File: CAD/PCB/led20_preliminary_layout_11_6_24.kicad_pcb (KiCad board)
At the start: 2 copper layers, 55 x 55 mm, 33 parts, among them U3 Battery, U6 JST

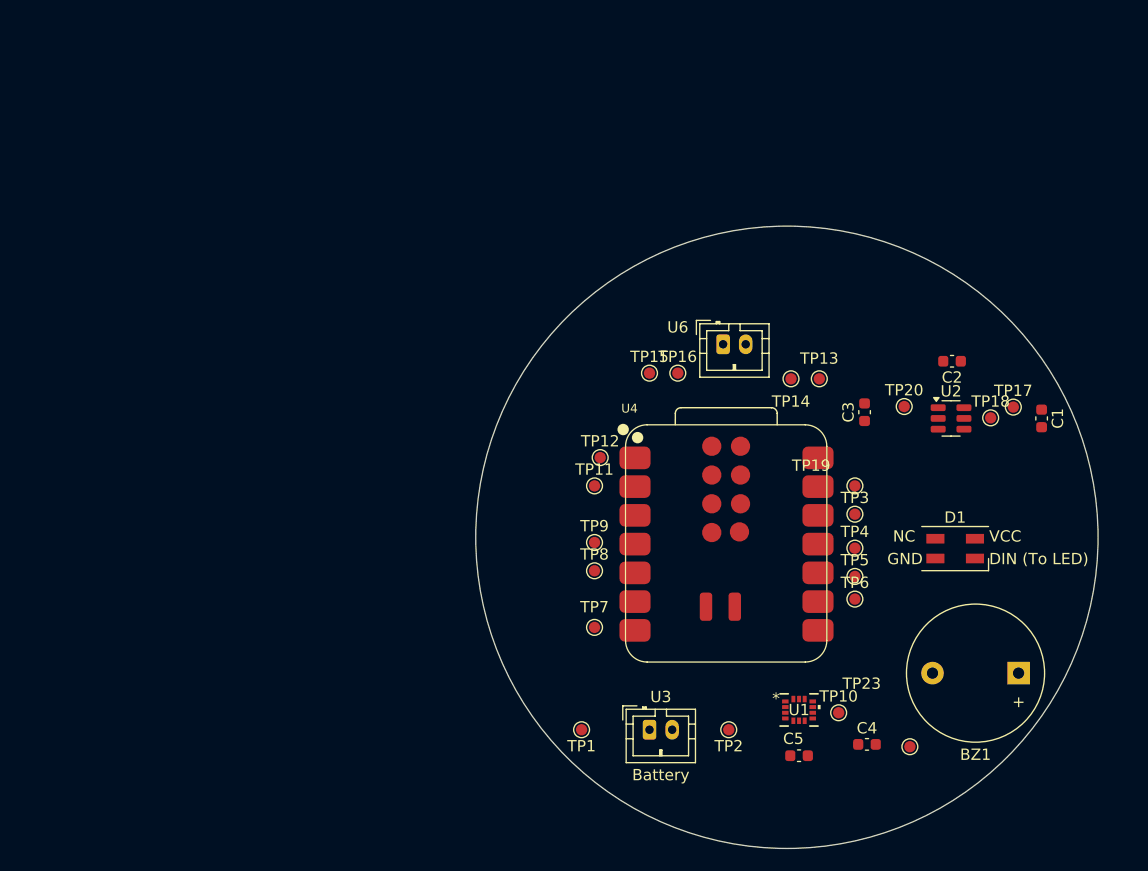
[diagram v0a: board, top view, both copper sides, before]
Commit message: Added Functional Decomposition
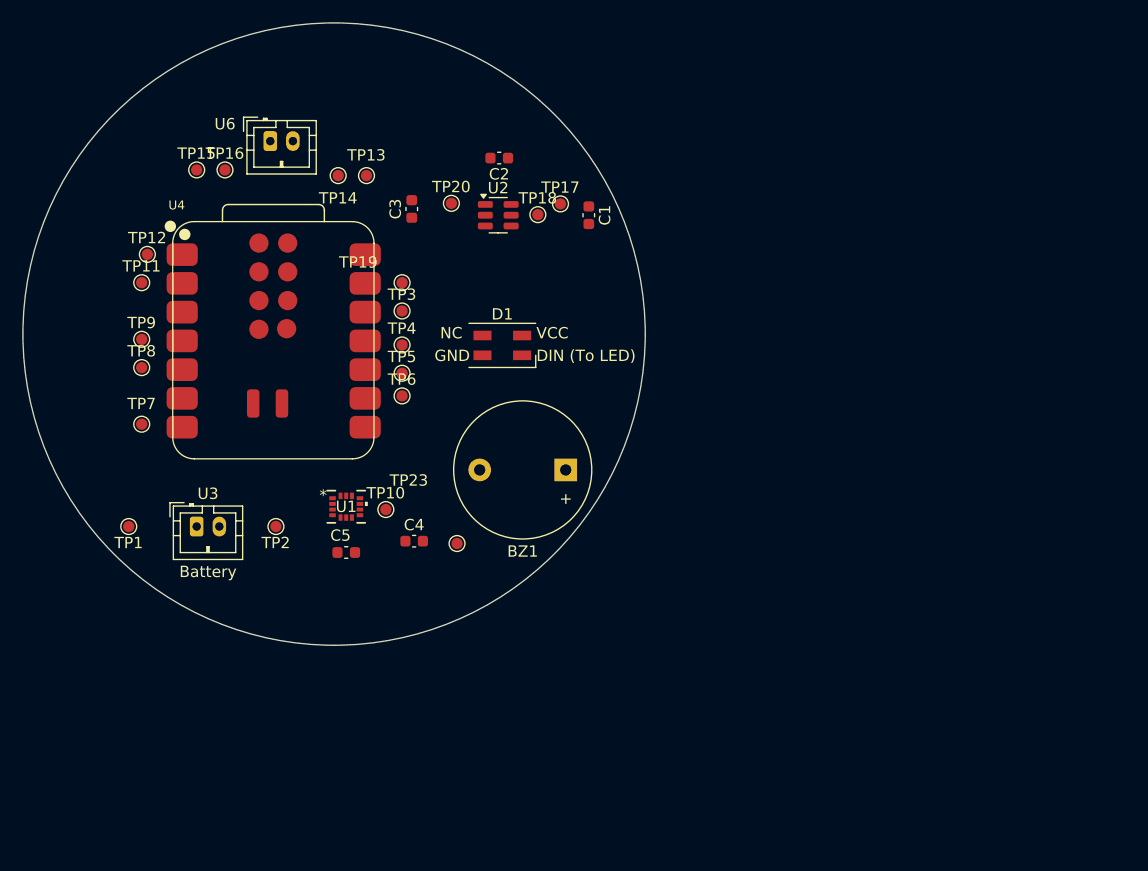
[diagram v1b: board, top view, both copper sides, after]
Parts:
- moved BZ1 43.8 mm to (123.6, 72.0)
- moved C2 43.8 mm to (117.7, 44.5)
- moved C3 43.8 mm to (110.0, 49.0)
- moved D1 43.8 mm to (118.0, 61.0)
- moved TP1 43.8 mm to (85.0, 77.0)
- moved TP11 43.8 mm to (86.1, 55.5)
- moved TP12 43.8 mm to (86.6, 53.0)
- moved TP13 43.8 mm to (106.0, 46.0)
- moved TP14 43.8 mm to (103.5, 46.0)
- moved TP15 43.8 mm to (91.0, 45.5)
- moved TP16 43.8 mm to (93.5, 45.5)
- moved TP2 43.8 mm to (98.0, 77.0)
- moved TP20 43.8 mm to (113.5, 48.5)
- moved TP23 43.8 mm to (114.0, 78.5)
- moved TP7 43.8 mm to (86.1, 68.0)
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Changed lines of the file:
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@@
 		(legacy_teardrops no)
 	)
-	(paper "A4")
+	(paper "A5")
 	(title_block
 		(title "LED20 Preliminary PCB Layout")
@@
 		(allow_soldermask_bridges_in_footprints no)
 		(pcbplotparams
-			(layerselection 0x0040000_7ffffffe)
+			(layerselection 0x0001000_7ffffffe)
 			(plot_on_all_layers_selection 0x7ffffff_80000001)
 			(disableapertmacros no)
@@
 			(drillshape 0)
 			(scaleselection 1)
-			(outputdirectory "")
+			(outputdirectory "./")
 		)
 	)
@@
 	(footprint "Connector_JST:JST_PH_B2B-PH-K_1x02_P2.00mm_Vertical"
 		(layer "F.Cu")
-		(at 137.5 60.95)
+		(at 97.5 43)
 		(descr "JST PH series connector, B2B-PH-K (http://www.jst-mfg.com/product/pdf/eng/ePH.pdf), generated with kicad-footprint-generator")
 		(tags "connector JST PH side entry")
@@
 	(footprint "TestPoint:TestPoint_Pad_D1.0mm"
 		(layer "F.Cu")
-		(at 138 95 180)
+		(at 98 77.05 180)
 		(descr "SMD pad as test Point, diameter 1.0mm")
 		(tags "test point SMD pad")
@@
 	(footprint "Led20:ChargePump"
 		(layer "F.Cu")
-		(at 157.6375 67.5)
+		(at 117.6375 49.55)
 		(descr "SOT, 6 Pin (~), generated with kicad-footprint-generator ipc_gullwing_generator.py")
 		(tags "SOT TO_SOT_SMD")
@@
 	(footprint "TestPoint:TestPoint_Pad_D1.0mm"
 		(layer "F.Cu")
-		(at 147.7103 93.499999)
+		(at 107.7103 75.549999)
 		(descr "SMD pad as test Point, diameter 1.0mm")
 		(tags "test point SMD pad")
@@
 	(footprint "TestPoint:TestPoint_Pad_D1.0mm"
 		(layer "F.Cu")
-		(at 154 96.5)
+		(at 114 78.55)
 		(descr "SMD pad as test Point, diameter 1.0mm")
 		(tags "test point SMD pad")
@@
 	(footprint "LED_SMD:LED_SK6812MINI_PLCC4_3.5x3.5mm_P1.75mm"
 		(layer "F.Cu")
-		(at 158 79)
+		(at 118 61.05)
 		(descr "3.5mm x 3.5mm PLCC4 Addressable RGB LED NeoPixel, https://cdn-shop.adafruit.com/product-files/2686/SK6812MINI_REV.01-1-2.pdf")
 		(tags "LED RGB NeoPixel Mini PLCC-4 3535")
@@
 	(footprint "Capacitor_SMD:C_0603_1608Metric"
 		(layer "F.Cu")
-		(at 150 66.95 90)
+		(at 110 49 90)
 		(descr "Capacitor SMD 0603 (1608 Metric), square (rectangular) end terminal, IPC_7351 nominal, (Body size source: IPC-SM-782 page 76, https://www.pcb-3d.com/wordpress/wp-content/uploads/ipc-sm-782a_amendment_1_and_2.pdf), generated with kicad-footprint-generator")
 		(tags "capacitor")
@@
 	(footprint "TestPoint:TestPoint_Pad_D1.0mm"
 		(layer "F.Cu")
-		(at 126.1444 80.96)
+		(at 86.1444 63.01)
 		(descr "SMD pad as test Point, diameter 1.0mm")
 		(tags "test point SMD pad")
@@
 	(footprint "TestPoint:TestPoint_Pad_D1.0mm"
 		(layer "F.Cu")
-		(at 131 63.5)
+		(at 91 45.55)
 		(descr "SMD pad as test Point, diameter 1.0mm")
 		(tags "test point SMD pad")
@@
 	(footprint "Connector_JST:JST_PH_B2B-PH-K_1x02_P2.00mm_Vertical"
 		(layer "F.Cu")
-		(at 131 95)
+		(at 91 77.05)
 		(descr "JST PH series connector, B2B-PH-K (http://www.jst-mfg.com/product/pdf/eng/ePH.pdf), generated with kicad-footprint-generator")
 		(tags "connector JST PH side entry")
@@
 	(footprint "TestPoint:TestPoint_Pad_D1.0mm"
 		(layer "F.Cu")
-		(at 133.5 63.5)
+		(at 93.5 45.55)
 		(descr "SMD pad as test Point, diameter 1.0mm")
 		(tags "test point SMD pad")
@@
 	(footprint "Capacitor_SMD:C_0603_1608Metric"
 		(layer "F.Cu")
-		(at 144.2103 97.293699)
+		(at 104.2103 79.343699)
 		(descr "Capacitor SMD 0603 (1608 Metric), square (rectangular) end terminal, IPC_7351 nominal, (Body size source: IPC-SM-782 page 76, https://www.pcb-3d.com/wordpress/wp-content/uploads/ipc-sm-782a_amendment_1_and_2.pdf), generated with kicad-footprint-generator")
 		(tags "capacitor")
@@
 	(footprint "Led20:LGA-14L_2P5X3X0P83_STM-L"
 		(layer "F.Cu")
-		(at 144.2103 93.249999)
+		(at 104.2103 75.299999)
 		(tags "LSM6DSO32TR ")
 		(property "Reference" "U1"
@@
 	(footprint "TestPoint:TestPoint_Pad_D1.0mm"
 		(layer "F.Cu")
-		(at 126.1444 85.96)
+		(at 86.1444 68.01)
 		(descr "SMD pad as test Point, diameter 1.0mm")
 		(tags "test point SMD pad")
@@
 	(footprint "Led20:XIAO-ESP32-C6-SMD"
 		(layer "F.Cu")
-		(at 138 78.58)
+		(at 98 60.63)
 		(property "Reference" "U4"
 			(at -9.5 -11.5 0)
@@
 	(footprint "TestPoint:TestPoint_Pad_D1.0mm"
 		(layer "F.Cu")
-		(at 146 64)
+		(at 106 46.05)
 		(descr "SMD pad as test Point, diameter 1.0mm")
 		(tags "test point SMD pad")
@@
 	(footprint "TestPoint:TestPoint_Pad_D1.0mm"
 		(layer "F.Cu")
-		(at 161.1375 67.45)
+		(at 121.1375 49.5)
 		(descr "SMD pad as test Point, diameter 1.0mm")
 		(tags "test point SMD pad")
@@
 	(footprint "Capacitor_SMD:C_0603_1608Metric"
 		(layer "F.Cu")
-		(at 165.6375 67.5 -90)
+		(at 125.6375 49.55 -90)
 		(descr "Capacitor SMD 0603 (1608 Metric), square (rectangular) end terminal, IPC_7351 nominal, (Body size source: IPC-SM-782 page 76, https://www.pcb-3d.com/wordpress/wp-content/uploads/ipc-sm-782a_amendment_1_and_2.pdf), generated with kicad-footprint-generator")
 		(tags "capacitor")
@@
 	(footprint "Buzzer_Beeper:Buzzer_12x9.5RM7.6"
 		(layer "F.Cu")
-		(at 163.6 90 180)
+		(at 123.6 72.05 180)
 		(descr "Generic Buzzer, D12mm height 9.5mm with RM7.6mm")
 		(tags "buzzer")
@@
 	(footprint "TestPoint:TestPoint_Pad_D1.0mm"
 		(layer "F.Cu")
-		(at 143.5 64)
+		(at 103.5 46.05)
 		(descr "SMD pad as test Point, diameter 1.0mm")
 		(tags "test point SMD pad")
@@
 	(footprint "TestPoint:TestPoint_Pad_D1.0mm"
 		(layer "F.Cu")
-		(at 125 95 180)
+		(at 85 77.05 180)
 		(descr "SMD pad as test Point, diameter 1.0mm")
 		(tags "test point SMD pad")
@@
 	(footprint "Capacitor_SMD:C_0603_1608Metric"
 		(layer "F.Cu")
-		(at 157.725 62.45 180)
+		(at 117.725 44.5 180)
 		(descr "Capacitor SMD 0603 (1608 Metric), square (rectangular) end terminal, IPC_7351 nominal, (Body size source: IPC-SM-782 page 76, https://www.pcb-3d.com/wordpress/wp-content/uploads/ipc-sm-782a_amendment_1_and_2.pdf), generated with kicad-footprint-generator")
 		(tags "capacitor")
@@
 	(footprint "TestPoint:TestPoint_Pad_D1.0mm"
 		(layer "F.Cu")
-		(at 163.1375 66.5)
+		(at 123.1375 48.55)
 		(descr "SMD pad as test Point, diameter 1.0mm")
 		(tags "test point SMD pad")
@@
 	(footprint "TestPoint:TestPoint_Pad_D1.0mm"
 		(layer "F.Cu")
-		(at 149.1444 78.96)
+		(at 109.1444 61.01)
 		(descr "SMD pad as test Point, diameter 1.0mm")
 		(tags "test point SMD pad")
@@
 	(footprint "TestPoint:TestPoint_Pad_D1.0mm"
 		(layer "F.Cu")
-		(at 153.5 66.45)
+		(at 113.5 48.5)
 		(descr "SMD pad as test Point, diameter 1.0mm")
 		(tags "test point SMD pad")
@@
 	(footprint "TestPoint:TestPoint_Pad_D1.0mm"
 		(layer "F.Cu")
-		(at 149.1444 75.96)
+		(at 109.1444 58.01)
 		(descr "SMD pad as test Point, diameter 1.0mm")
 		(tags "test point SMD pad")
@@
 	(footprint "TestPoint:TestPoint_Pad_D1.0mm"
 		(layer "F.Cu")
-		(at 149.1444 73.46)
+		(at 109.1444 55.51)
 		(descr "SMD pad as test Point, diameter 1.0mm")
 		(tags "test point SMD pad")
@@
 	(footprint "TestPoint:TestPoint_Pad_D1.0mm"
 		(layer "F.Cu")
-		(at 149.1444 83.46)
+		(at 109.1444 65.51)
 		(descr "SMD pad as test Point, diameter 1.0mm")
 		(tags "test point SMD pad")
@@
 	(footprint "TestPoint:TestPoint_Pad_D1.0mm"
 		(layer "F.Cu")
-		(at 126.6444 70.96)
+		(at 86.6444 53.01)
 		(descr "SMD pad as test Point, diameter 1.0mm")
 		(tags "test point SMD pad")
@@
 	(footprint "TestPoint:TestPoint_Pad_D1.0mm"
 		(layer "F.Cu")
-		(at 126.1444 73.46)
+		(at 86.1444 55.51)
 		(descr "SMD pad as test Point, diameter 1.0mm")
 		(tags "test point SMD pad")
@@
 	(footprint "TestPoint:TestPoint_Pad_D1.0mm"
 		(layer "F.Cu")
-		(at 149.1444 81.46)
+		(at 109.1444 63.51)
 		(descr "SMD pad as test Point, diameter 1.0mm")
 		(tags "test point SMD pad")
@@
 	(footprint "TestPoint:TestPoint_Pad_D1.0mm"
 		(layer "F.Cu")
-		(at 126.1444 78.46)
+		(at 86.1444 60.51)
 		(descr "SMD pad as test Point, diameter 1.0mm")
 		(tags "test point SMD pad")
@@
 	(footprint "Capacitor_SMD:C_0603_1608Metric"
 		(layer "F.Cu")
-		(at 150.2103 96.293699)
+		(at 110.2103 78.343699)
 		(descr "Capacitor SMD 0603 (1608 Metric), square (rectangular) end terminal, IPC_7351 nominal, (Body size source: IPC-SM-782 page 76, https://www.pcb-3d.com/wordpress/wp-content/uploads/ipc-sm-782a_amendment_1_and_2.pdf), generated with kicad-footprint-generator")
 		(tags "capacitor")
@@
 	)
 	(gr_circle
-		(center 143.1375 78)
-		(end 163 59)
+		(center 103.1375 60.05)
+		(end 123 41.05)
 		(stroke
 			(width 0.05)
@@
 	)
 	(gr_text "NC"
-		(at 152.5 78.5 0)
+		(at 112.5 60.55 0)
 		(layer "F.SilkS")
 		(effects
@@
 	)
 	(gr_text "DIN (To LED)\n"
-		(at 161 80.5 0)
+		(at 121 62.55 0)
 		(layer "F.SilkS")
 		(effects
@@
 	)
 	(gr_text "GND\n"
-		(at 152 80.5 0)
+		(at 112 62.55 0)
 		(layer "F.SilkS")
 		(effects
@@
 	)
 	(gr_text "VCC"
-		(at 161 78.5 0)
+		(at 121 60.55 0)
 		(layer "F.SilkS")
 		(effects

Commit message: Resubmit
see previous notes
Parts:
- moved BZ1 43.8 mm to (163.6, 90.0)
- moved C2 43.8 mm to (157.7, 62.5)
- moved C3 43.8 mm to (150.0, 67.0)
- moved D1 43.8 mm to (158.0, 79.0)
- moved TP1 43.8 mm to (125.0, 95.0)
- moved TP11 43.8 mm to (126.1, 73.5)
- moved TP12 43.8 mm to (126.6, 71.0)
- moved TP13 43.8 mm to (146.0, 64.0)
- moved TP14 43.8 mm to (143.5, 64.0)
- moved TP15 43.8 mm to (131.0, 63.5)
- moved TP16 43.8 mm to (133.5, 63.5)
- moved TP2 43.8 mm to (138.0, 95.0)
- moved TP20 43.8 mm to (153.5, 66.5)
- moved TP23 43.8 mm to (154.0, 96.5)
- moved TP7 43.8 mm to (126.1, 86.0)
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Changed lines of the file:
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@@
 		(legacy_teardrops no)
 	)
-	(paper "A5")
+	(paper "A4")
 	(title_block
 		(title "LED20 Preliminary PCB Layout")
@@
 		(allow_soldermask_bridges_in_footprints no)
 		(pcbplotparams
-			(layerselection 0x0001000_7ffffffe)
+			(layerselection 0x0040000_7ffffffe)
 			(plot_on_all_layers_selection 0x7ffffff_80000001)
 			(disableapertmacros no)
@@
 			(drillshape 0)
 			(scaleselection 1)
-			(outputdirectory "./")
+			(outputdirectory "")
 		)
 	)
@@
 	(footprint "Connector_JST:JST_PH_B2B-PH-K_1x02_P2.00mm_Vertical"
 		(layer "F.Cu")
-		(at 97.5 43)
+		(at 137.5 60.95)
 		(descr "JST PH series connector, B2B-PH-K (http://www.jst-mfg.com/product/pdf/eng/ePH.pdf), generated with kicad-footprint-generator")
 		(tags "connector JST PH side entry")
@@
 	(footprint "TestPoint:TestPoint_Pad_D1.0mm"
 		(layer "F.Cu")
-		(at 98 77.05 180)
+		(at 138 95 180)
 		(descr "SMD pad as test Point, diameter 1.0mm")
 		(tags "test point SMD pad")
@@
 	(footprint "Led20:ChargePump"
 		(layer "F.Cu")
-		(at 117.6375 49.55)
+		(at 157.6375 67.5)
 		(descr "SOT, 6 Pin (~), generated with kicad-footprint-generator ipc_gullwing_generator.py")
 		(tags "SOT TO_SOT_SMD")
@@
 	(footprint "TestPoint:TestPoint_Pad_D1.0mm"
 		(layer "F.Cu")
-		(at 107.7103 75.549999)
+		(at 147.7103 93.499999)
 		(descr "SMD pad as test Point, diameter 1.0mm")
 		(tags "test point SMD pad")
@@
 	(footprint "TestPoint:TestPoint_Pad_D1.0mm"
 		(layer "F.Cu")
-		(at 114 78.55)
+		(at 154 96.5)
 		(descr "SMD pad as test Point, diameter 1.0mm")
 		(tags "test point SMD pad")
@@
 	(footprint "LED_SMD:LED_SK6812MINI_PLCC4_3.5x3.5mm_P1.75mm"
 		(layer "F.Cu")
-		(at 118 61.05)
+		(at 158 79)
 		(descr "3.5mm x 3.5mm PLCC4 Addressable RGB LED NeoPixel, https://cdn-shop.adafruit.com/product-files/2686/SK6812MINI_REV.01-1-2.pdf")
 		(tags "LED RGB NeoPixel Mini PLCC-4 3535")
@@
 	(footprint "Capacitor_SMD:C_0603_1608Metric"
 		(layer "F.Cu")
-		(at 110 49 90)
+		(at 150 66.95 90)
 		(descr "Capacitor SMD 0603 (1608 Metric), square (rectangular) end terminal, IPC_7351 nominal, (Body size source: IPC-SM-782 page 76, https://www.pcb-3d.com/wordpress/wp-content/uploads/ipc-sm-782a_amendment_1_and_2.pdf), generated with kicad-footprint-generator")
 		(tags "capacitor")
@@
 	(footprint "TestPoint:TestPoint_Pad_D1.0mm"
 		(layer "F.Cu")
-		(at 86.1444 63.01)
+		(at 126.1444 80.96)
 		(descr "SMD pad as test Point, diameter 1.0mm")
 		(tags "test point SMD pad")
@@
 	(footprint "TestPoint:TestPoint_Pad_D1.0mm"
 		(layer "F.Cu")
-		(at 91 45.55)
+		(at 131 63.5)
 		(descr "SMD pad as test Point, diameter 1.0mm")
 		(tags "test point SMD pad")
@@
 	(footprint "Connector_JST:JST_PH_B2B-PH-K_1x02_P2.00mm_Vertical"
 		(layer "F.Cu")
-		(at 91 77.05)
+		(at 131 95)
 		(descr "JST PH series connector, B2B-PH-K (http://www.jst-mfg.com/product/pdf/eng/ePH.pdf), generated with kicad-footprint-generator")
 		(tags "connector JST PH side entry")
@@
 	(footprint "TestPoint:TestPoint_Pad_D1.0mm"
 		(layer "F.Cu")
-		(at 93.5 45.55)
+		(at 133.5 63.5)
 		(descr "SMD pad as test Point, diameter 1.0mm")
 		(tags "test point SMD pad")
@@
 	(footprint "Capacitor_SMD:C_0603_1608Metric"
 		(layer "F.Cu")
-		(at 104.2103 79.343699)
+		(at 144.2103 97.293699)
 		(descr "Capacitor SMD 0603 (1608 Metric), square (rectangular) end terminal, IPC_7351 nominal, (Body size source: IPC-SM-782 page 76, https://www.pcb-3d.com/wordpress/wp-content/uploads/ipc-sm-782a_amendment_1_and_2.pdf), generated with kicad-footprint-generator")
 		(tags "capacitor")
@@
 	(footprint "Led20:LGA-14L_2P5X3X0P83_STM-L"
 		(layer "F.Cu")
-		(at 104.2103 75.299999)
+		(at 144.2103 93.249999)
 		(tags "LSM6DSO32TR ")
 		(property "Reference" "U1"
@@
 	(footprint "TestPoint:TestPoint_Pad_D1.0mm"
 		(layer "F.Cu")
-		(at 86.1444 68.01)
+		(at 126.1444 85.96)
 		(descr "SMD pad as test Point, diameter 1.0mm")
 		(tags "test point SMD pad")
@@
 	(footprint "Led20:XIAO-ESP32-C6-SMD"
 		(layer "F.Cu")
-		(at 98 60.63)
+		(at 138 78.58)
 		(property "Reference" "U4"
 			(at -9.5 -11.5 0)
@@
 	(footprint "TestPoint:TestPoint_Pad_D1.0mm"
 		(layer "F.Cu")
-		(at 106 46.05)
+		(at 146 64)
 		(descr "SMD pad as test Point, diameter 1.0mm")
 		(tags "test point SMD pad")
@@
 	(footprint "TestPoint:TestPoint_Pad_D1.0mm"
 		(layer "F.Cu")
-		(at 121.1375 49.5)
+		(at 161.1375 67.45)
 		(descr "SMD pad as test Point, diameter 1.0mm")
 		(tags "test point SMD pad")
@@
 	(footprint "Capacitor_SMD:C_0603_1608Metric"
 		(layer "F.Cu")
-		(at 125.6375 49.55 -90)
+		(at 165.6375 67.5 -90)
 		(descr "Capacitor SMD 0603 (1608 Metric), square (rectangular) end terminal, IPC_7351 nominal, (Body size source: IPC-SM-782 page 76, https://www.pcb-3d.com/wordpress/wp-content/uploads/ipc-sm-782a_amendment_1_and_2.pdf), generated with kicad-footprint-generator")
 		(tags "capacitor")
@@
 	(footprint "Buzzer_Beeper:Buzzer_12x9.5RM7.6"
 		(layer "F.Cu")
-		(at 123.6 72.05 180)
+		(at 163.6 90 180)
 		(descr "Generic Buzzer, D12mm height 9.5mm with RM7.6mm")
 		(tags "buzzer")
@@
 	(footprint "TestPoint:TestPoint_Pad_D1.0mm"
 		(layer "F.Cu")
-		(at 103.5 46.05)
+		(at 143.5 64)
 		(descr "SMD pad as test Point, diameter 1.0mm")
 		(tags "test point SMD pad")
@@
 	(footprint "TestPoint:TestPoint_Pad_D1.0mm"
 		(layer "F.Cu")
-		(at 85 77.05 180)
+		(at 125 95 180)
 		(descr "SMD pad as test Point, diameter 1.0mm")
 		(tags "test point SMD pad")
@@
 	(footprint "Capacitor_SMD:C_0603_1608Metric"
 		(layer "F.Cu")
-		(at 117.725 44.5 180)
+		(at 157.725 62.45 180)
 		(descr "Capacitor SMD 0603 (1608 Metric), square (rectangular) end terminal, IPC_7351 nominal, (Body size source: IPC-SM-782 page 76, https://www.pcb-3d.com/wordpress/wp-content/uploads/ipc-sm-782a_amendment_1_and_2.pdf), generated with kicad-footprint-generator")
 		(tags "capacitor")
@@
 	(footprint "TestPoint:TestPoint_Pad_D1.0mm"
 		(layer "F.Cu")
-		(at 123.1375 48.55)
+		(at 163.1375 66.5)
 		(descr "SMD pad as test Point, diameter 1.0mm")
 		(tags "test point SMD pad")
@@
 	(footprint "TestPoint:TestPoint_Pad_D1.0mm"
 		(layer "F.Cu")
-		(at 109.1444 61.01)
+		(at 149.1444 78.96)
 		(descr "SMD pad as test Point, diameter 1.0mm")
 		(tags "test point SMD pad")
@@
 	(footprint "TestPoint:TestPoint_Pad_D1.0mm"
 		(layer "F.Cu")
-		(at 113.5 48.5)
+		(at 153.5 66.45)
 		(descr "SMD pad as test Point, diameter 1.0mm")
 		(tags "test point SMD pad")
@@
 	(footprint "TestPoint:TestPoint_Pad_D1.0mm"
 		(layer "F.Cu")
-		(at 109.1444 58.01)
+		(at 149.1444 75.96)
 		(descr "SMD pad as test Point, diameter 1.0mm")
 		(tags "test point SMD pad")
@@
 	(footprint "TestPoint:TestPoint_Pad_D1.0mm"
 		(layer "F.Cu")
-		(at 109.1444 55.51)
+		(at 149.1444 73.46)
 		(descr "SMD pad as test Point, diameter 1.0mm")
 		(tags "test point SMD pad")
@@
 	(footprint "TestPoint:TestPoint_Pad_D1.0mm"
 		(layer "F.Cu")
-		(at 109.1444 65.51)
+		(at 149.1444 83.46)
 		(descr "SMD pad as test Point, diameter 1.0mm")
 		(tags "test point SMD pad")
@@
 	(footprint "TestPoint:TestPoint_Pad_D1.0mm"
 		(layer "F.Cu")
-		(at 86.6444 53.01)
+		(at 126.6444 70.96)
 		(descr "SMD pad as test Point, diameter 1.0mm")
 		(tags "test point SMD pad")
@@
 	(footprint "TestPoint:TestPoint_Pad_D1.0mm"
 		(layer "F.Cu")
-		(at 86.1444 55.51)
+		(at 126.1444 73.46)
 		(descr "SMD pad as test Point, diameter 1.0mm")
 		(tags "test point SMD pad")
@@
 	(footprint "TestPoint:TestPoint_Pad_D1.0mm"
 		(layer "F.Cu")
-		(at 109.1444 63.51)
+		(at 149.1444 81.46)
 		(descr "SMD pad as test Point, diameter 1.0mm")
 		(tags "test point SMD pad")
@@
 	(footprint "TestPoint:TestPoint_Pad_D1.0mm"
 		(layer "F.Cu")
-		(at 86.1444 60.51)
+		(at 126.1444 78.46)
 		(descr "SMD pad as test Point, diameter 1.0mm")
 		(tags "test point SMD pad")
@@
 	(footprint "Capacitor_SMD:C_0603_1608Metric"
 		(layer "F.Cu")
-		(at 110.2103 78.343699)
+		(at 150.2103 96.293699)
 		(descr "Capacitor SMD 0603 (1608 Metric), square (rectangular) end terminal, IPC_7351 nominal, (Body size source: IPC-SM-782 page 76, https://www.pcb-3d.com/wordpress/wp-content/uploads/ipc-sm-782a_amendment_1_and_2.pdf), generated with kicad-footprint-generator")
 		(tags "capacitor")
@@
 	)
 	(gr_circle
-		(center 103.1375 60.05)
-		(end 123 41.05)
+		(center 143.1375 78)
+		(end 163 59)
 		(stroke
 			(width 0.05)
@@
 	)
 	(gr_text "NC"
-		(at 112.5 60.55 0)
+		(at 152.5 78.5 0)
 		(layer "F.SilkS")
 		(effects
@@
 	)
 	(gr_text "DIN (To LED)\n"
-		(at 121 62.55 0)
+		(at 161 80.5 0)
 		(layer "F.SilkS")
 		(effects
@@
 	)
 	(gr_text "GND\n"
-		(at 112 62.55 0)
+		(at 152 80.5 0)
 		(layer "F.SilkS")
 		(effects
@@
 	)
 	(gr_text "VCC"
-		(at 121 60.55 0)
+		(at 161 78.5 0)
 		(layer "F.SilkS")
 		(effects
